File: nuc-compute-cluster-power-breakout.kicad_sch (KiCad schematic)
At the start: 44 parts, among them J10 10107844-002LF, J2 BM04B-SRSS-TB-LF-SN, J3 BM04B-SRSS-TB-LF-SN, J4 39288080, J5 39288080, J6 39288080, J7 39288080, J8 39288080, Q11 BC856,215

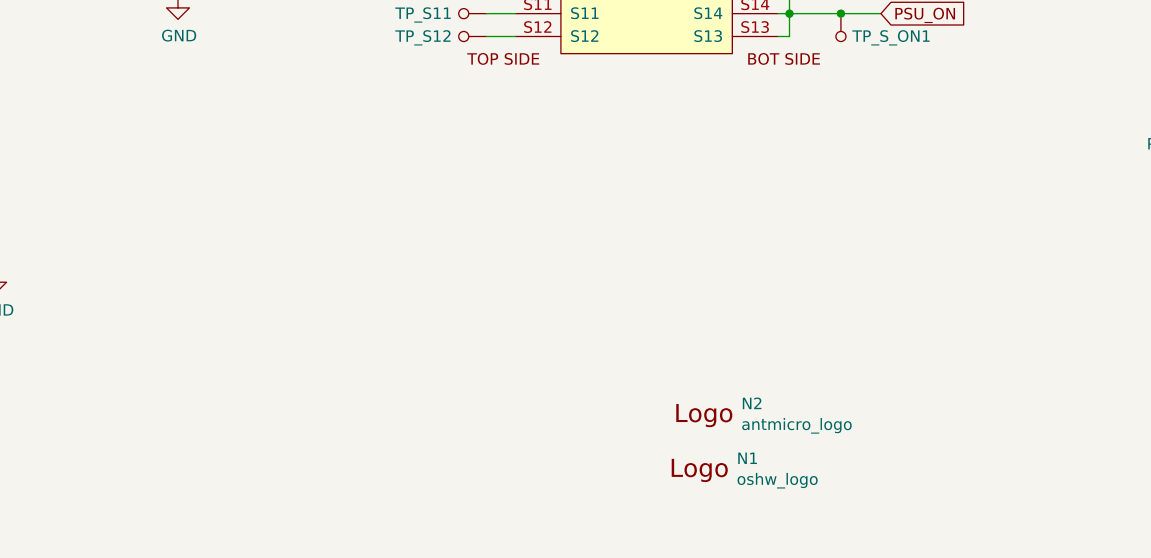
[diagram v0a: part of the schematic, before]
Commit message: Added LED indicators
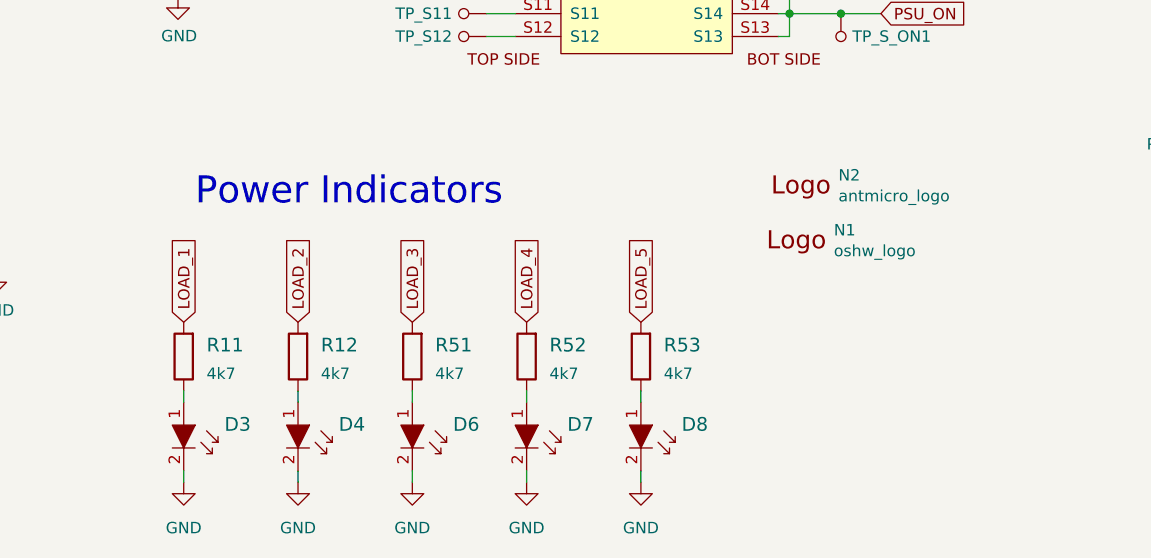
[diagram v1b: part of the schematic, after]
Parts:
- added D3, D4, D6, D7, D8: LG_L29K-G2J1-24-Z, nuc-compute-cluster-power-breakout-footprints:LED_0603, symbol nuc-compute-cluster-power-breakout:LG_L29K-G2J1-24-Z
- added R11, R12, R51, R52, R53: R_4k7_0603, antmicro-footprints:0603-res, symbol antmicroResistors0603:R_4k7_0603
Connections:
- net GND: now also D3.2, D4.2, D6.2, D7.2, D8.2
- net LOAD_1: now also R11.2
- net LOAD_2: now also R12.2
- net LOAD_3: now also R51.2
- net LOAD_4: now also R52.2
- net LOAD_5: now also R53.2
- new net: D8.1, R53.1
- new net: D6.1, R51.1
- new net: D3.1, R11.1
- new net: D4.1, R12.1
- new net: D7.1, R52.1
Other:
- note added: "Power Indicators"
- moved on the sheet: N1, N2

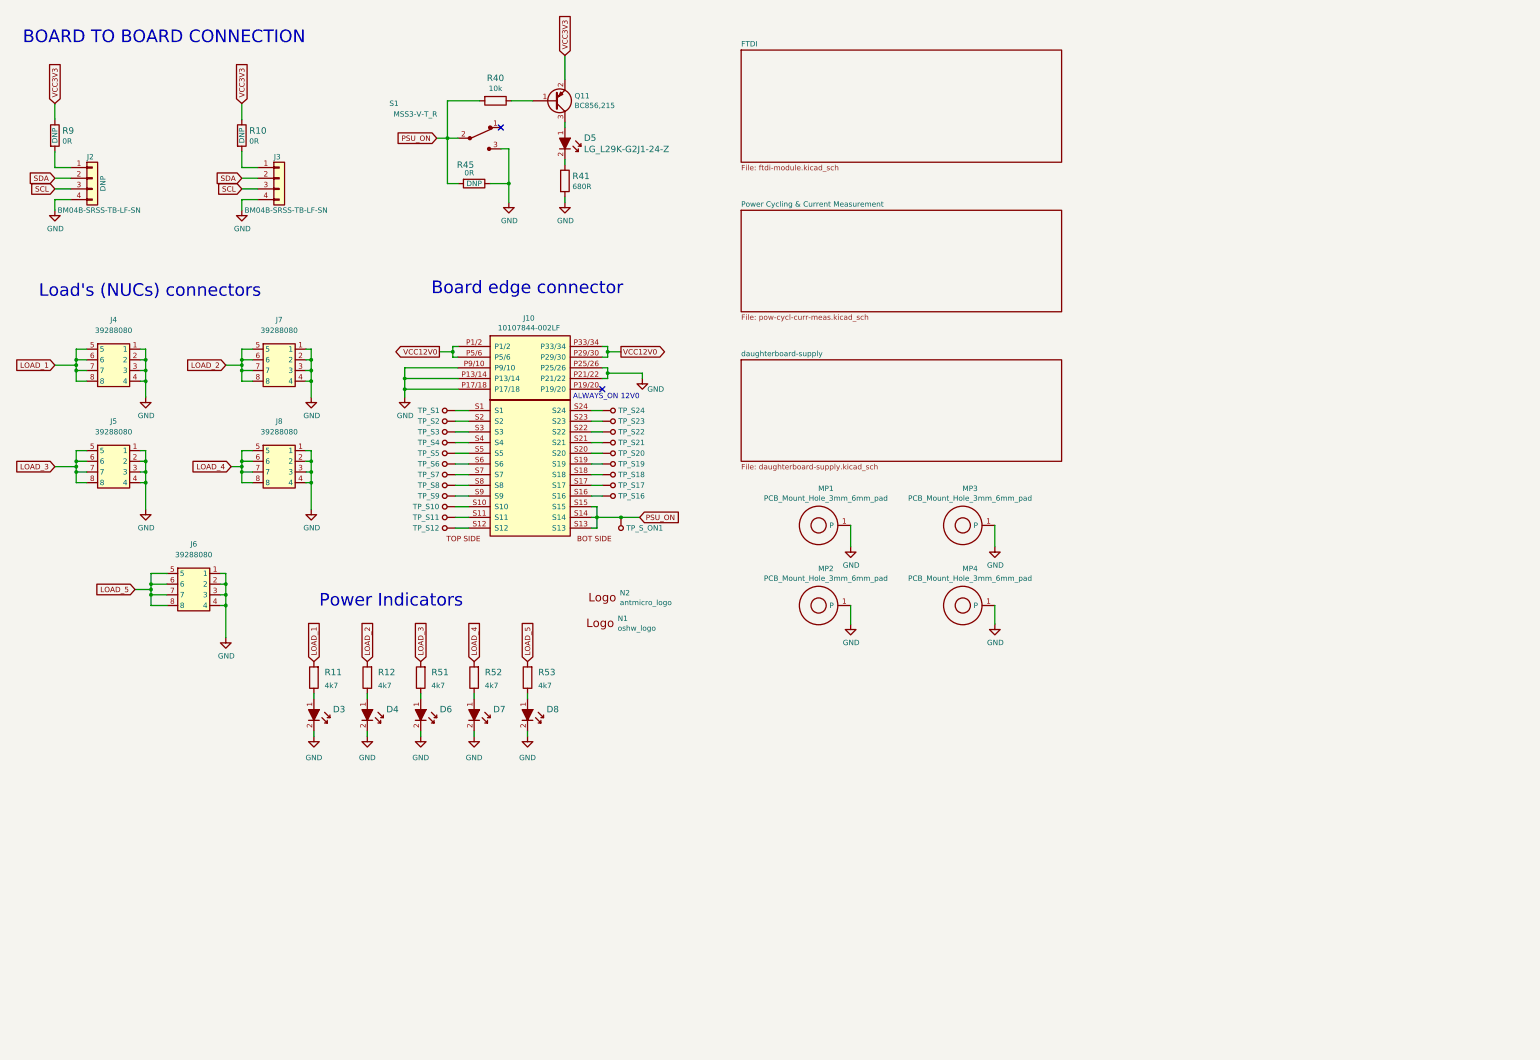
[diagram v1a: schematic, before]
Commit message: Added LED indicators for all voltage rails
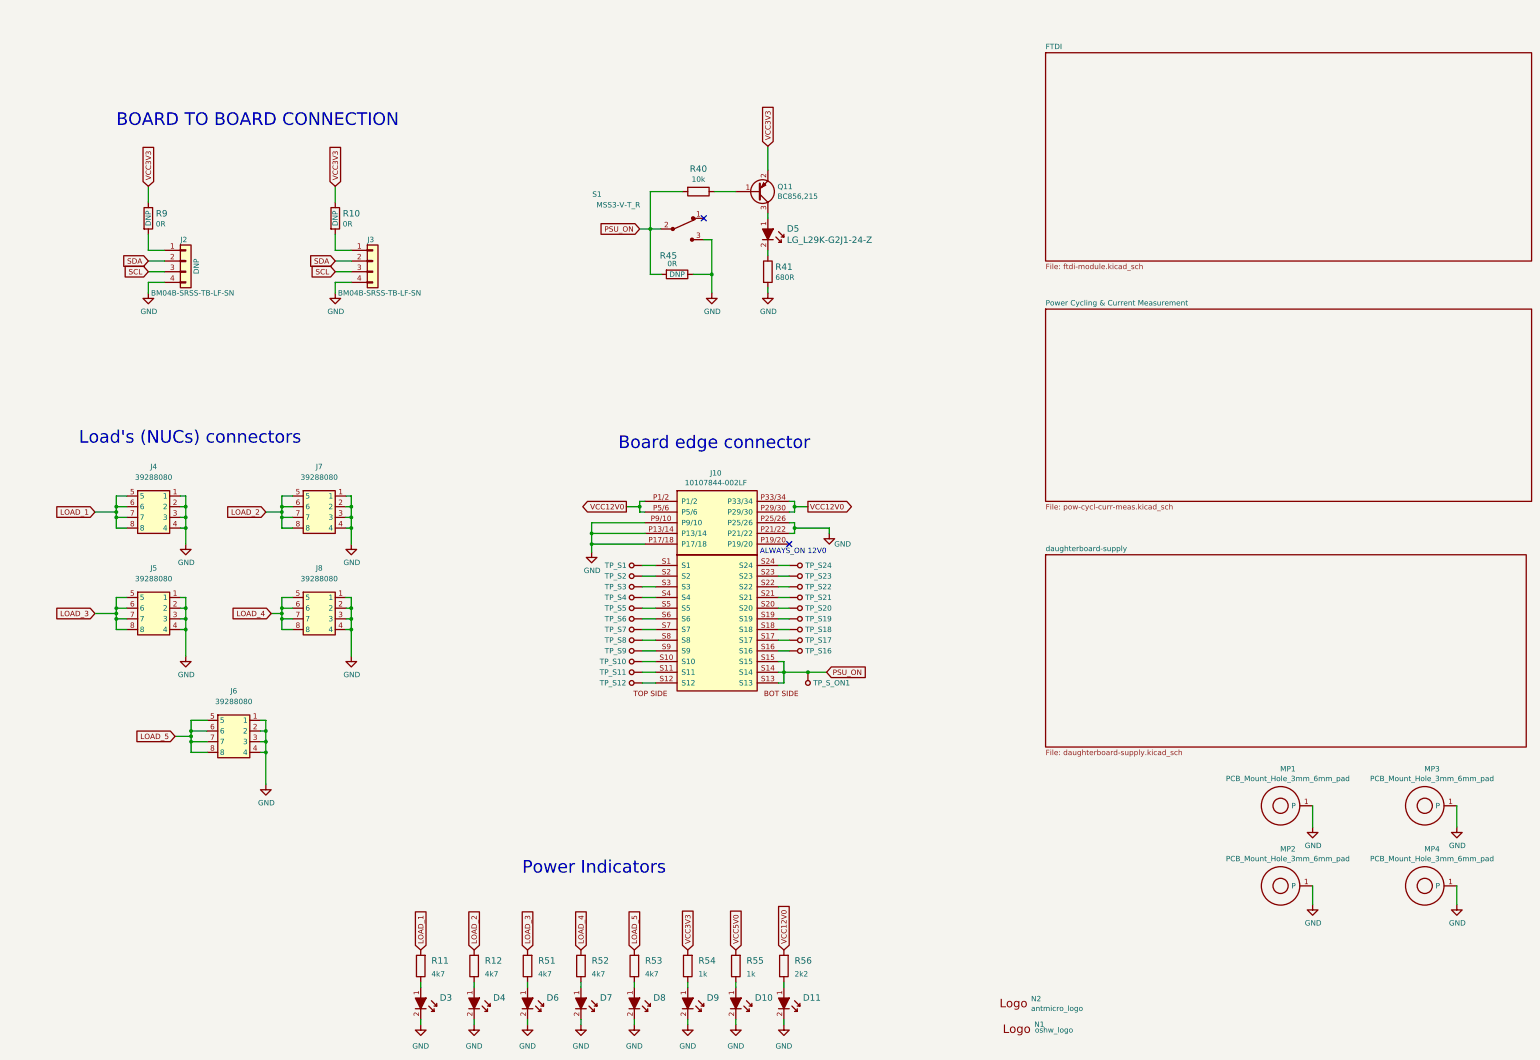
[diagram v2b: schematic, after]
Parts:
- added D10, D11, D9: LG_L29K-G2J1-24-Z, nuc-compute-cluster-power-breakout-footprints:LED_0603, symbol nuc-compute-cluster-power-breakout:LG_L29K-G2J1-24-Z
- added R54, R55: R_1k_0603, antmicro-footprints:0603-res, symbol antmicroResistors0603:R_1k_0603
- added R56: R_2k2_0603, antmicro-footprints:0603-res, symbol antmicroResistors0603:R_2k2_0603
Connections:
- net GND: now also D10.2, D11.2, D9.2
- net P3/4: now also R56.2
- net VCC3V3: now also R54.2
- new net: D10.1, R55.1
- new net: D11.1, R56.1
- new net: D9.1, R54.1
- new net VCC5V0: R55.2
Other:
- moved on the sheet: D3, D4, D5, D6, D7, D8, J10, J2, J3, J4, J5, J6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
